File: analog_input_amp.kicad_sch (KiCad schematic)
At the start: 32 parts, among them U601 THS4521ID

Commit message: Schematic: add PNs for resistors
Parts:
- R601: Mfr (none) -> Bourns; Mfr PN (none) -> CR0805-J/-000ELF
- R602: Mfr (none) -> Bourns; Mfr PN (none) -> CR0805-FX-49R9ELF
- R603, R604: Mfr (none) -> Bourns; Mfr PN (none) -> CR0805-FX-1001ELF
- R605: Mfr (none) -> Bourns; Mfr PN (none) -> CR0805-FX-62R0ELF
- R606, R608: Mfr (none) -> Bourns; Mfr PN (none) -> CR0805-FX-2000ELF
- R607: Mfr (none) -> Bourns; Mfr PN (none) -> CR0805-FX-27R0ELF
- R609, R610: Mfr (none) -> Bourns; Mfr PN (none) -> CR0805-FX-24R0ELF
- R611, R612: Mfr (none) -> Bourns; Mfr PN (none) -> CR0805-FX-2200ELF
- R613, R614: Mfr (none) -> Bourns; Mfr PN (none) -> CR0805-FX-1000ELF
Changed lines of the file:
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@@
+      (effects (font (size 1.27 1.27)) hide)
+    )
+    (property "Mfr" "Bourns" (id 5) (at 156.21 106.68 0)
+      (effects (font (size 1.27 1.27)) hide)
+    )
+    (property "Mfr PN" "CR0805-FX-24R0ELF" (id 6) (at 156.21 106.68 0)
       (effects (font (size 1.27 1.27)) hide)
     )
@@
       (effects (font (size 1.27 1.27)) hide)
     )
+    (property "Mfr" "Bourns" (id 5) (at 167.64 125.73 0)
+      (effects (font (size 1.27 1.27)) hide)
+    )
+    (property "Mfr PN" "CR0805-FX-2200ELF" (id 6) (at 167.64 125.73 0)
+      (effects (font (size 1.27 1.27)) hide)
+    )
     (pin "1")
     (pin "2")
@@
     )
     (property "Tolerance" "" (id 4) (at 76.2 91.44 0)
+      (effects (font (size 1.27 1.27)) hide)
+    )
+    (property "Mfr" "Bourns" (id 5) (at 76.2 91.44 0)
+      (effects (font (size 1.27 1.27)) hide)
+    )
+    (property "Mfr PN" "CR0805-FX-49R9ELF" (id 6) (at 76.2 91.44 0)
       (effects (font (size 1.27 1.27)) hide)
     )
@@
       (effects (font (size 1.27 1.27)) hide)
     )
+    (property "Mfr" "Bourns" (id 5) (at 127 106.68 0)
+      (effects (font (size 1.27 1.27)) hide)
+    )
+    (property "Mfr PN" "CR0805-FX-27R0ELF" (id 6) (at 127 106.68 0)
+      (effects (font (size 1.27 1.27)) hide)
+    )
     (pin "1")
     (pin "2")
@@
     )
     (property "Tolerance" "" (id 4) (at 88.9 158.75 0)
+      (effects (font (size 1.27 1.27)) hide)
+    )
+    (property "Mfr" "Bourns" (id 5) (at 88.9 158.75 0)
+      (effects (font (size 1.27 1.27)) hide)
+    )
+    (property "Mfr PN" "CR0805-FX-1001ELF" (id 6) (at 88.9 158.75 0)
       (effects (font (size 1.27 1.27)) hide)
     )
@@
       (effects (font (size 1.27 1.27)) hide)
     )
+    (property "Mfr" "Bourns" (id 5) (at 167.64 45.72 0)
+      (effects (font (size 1.27 1.27)) hide)
+    )
+    (property "Mfr PN" "CR0805-FX-2200ELF" (id 6) (at 167.64 45.72 0)
+      (effects (font (size 1.27 1.27)) hide)
+    )
     (pin "1")
     (pin "2")
@@
       (effects (font (size 1.27 1.27)) hide)
     )
+    (property "Mfr" "Bourns" (id 5) (at 156.21 63.5 0)
+      (effects (font (size 1.27 1.27)) hide)
+    )
+    (property "Mfr PN" "CR0805-FX-24R0ELF" (id 6) (at 156.21 63.5 0)
+      (effects (font (size 1.27 1.27)) hide)
+    )
     (pin "1")
     (pin "2")
@@
     )
     (property "Tolerance" "" (id 4) (at 196.85 106.68 0)
+      (effects (font (size 1.27 1.27)) hide)
+    )
+    (property "Mfr" "Bourns" (id 5) (at 196.85 106.68 0)
+      (effects (font (size 1.27 1.27)) hide)
+    )
+    (property "Mfr PN" "CR0805-FX-1000ELF" (id 6) (at 196.85 106.68 0)
       (effects (font (size 1.27 1.27)) hide)
     )
@@
       (effects (font (size 1.27 1.27)) hide)
     )
+    (property "Mfr" "Bourns" (id 5) (at 139.7 106.68 0)
+      (effects (font (size 1.27 1.27)) hide)
+    )
+    (property "Mfr PN" "CR0805-FX-2000ELF" (id 6) (at 139.7 106.68 0)
+      (effects (font (size 1.27 1.27)) hide)
+    )
     (pin "1")
     (pin "2")
@@
       (effects (font (size 1.27 1.27)) hide)
     )
+    (property "Mfr" "Bourns" (id 5) (at 127 63.5 0)
+      (effects (font (size 1.27 1.27)) hide)
+    )
+    (property "Mfr PN" "CR0805-FX-2000ELF" (id 6) (at 127 63.5 0)
+      (effects (font (size 1.27 1.27)) hide)
+    )
     (pin "1")
     (pin "2")
@@
     )
     (property "Datasheet" "~" (id 3) (at 63.5 146.05 0)
+      (effects (font (size 1.27 1.27)) hide)
+    )
+    (property "Mfr" "Bourns" (id 4) (at 63.5 146.05 0)
+      (effects (font (size 1.27 1.27)) hide)
+    )
+    (property "Mfr PN" "CR0805-J/-000ELF" (id 5) (at 63.5 146.05 0)
       (effects (font (size 1.27 1.27)) hide)
     )
@@
       (effects (font (size 1.27 1.27)) hide)
     )
+    (property "Mfr" "Bourns" (id 5) (at 196.85 63.5 0)
+      (effects (font (size 1.27 1.27)) hide)
+    )
+    (property "Mfr PN" "CR0805-FX-1000ELF" (id 6) (at 196.85 63.5 0)
+      (effects (font (size 1.27 1.27)) hide)
+    )
     (pin "1")
     (pin "2")
@@
     )
     (property "Tolerance" "" (id 4) (at 88.9 146.05 0)
+      (effects (font (size 1.27 1.27)) hide)
+    )
+    (property "Mfr" "Bourns" (id 5) (at 88.9 146.05 0)
+      (effects (font (size 1.27 1.27)) hide)
+    )
+    (property "Mfr PN" "CR0805-FX-1001ELF" (id 6) (at 88.9 146.05 0)
       (effects (font (size 1.27 1.27)) hide)
     )
@@
       (effects (font (size 1.27 1.27)) hide)
     )
+    (property "Mfr" "Bourns" (id 5) (at 101.6 85.09 0)
+      (effects (font (size 1.27 1.27)) hide)
+    )
+    (property "Mfr PN" "CR0805-FX-62R0ELF" (id 6) (at 101.6 85.09 0)
+      (effects (font (size 1.27 1.27)) hide)
+    )

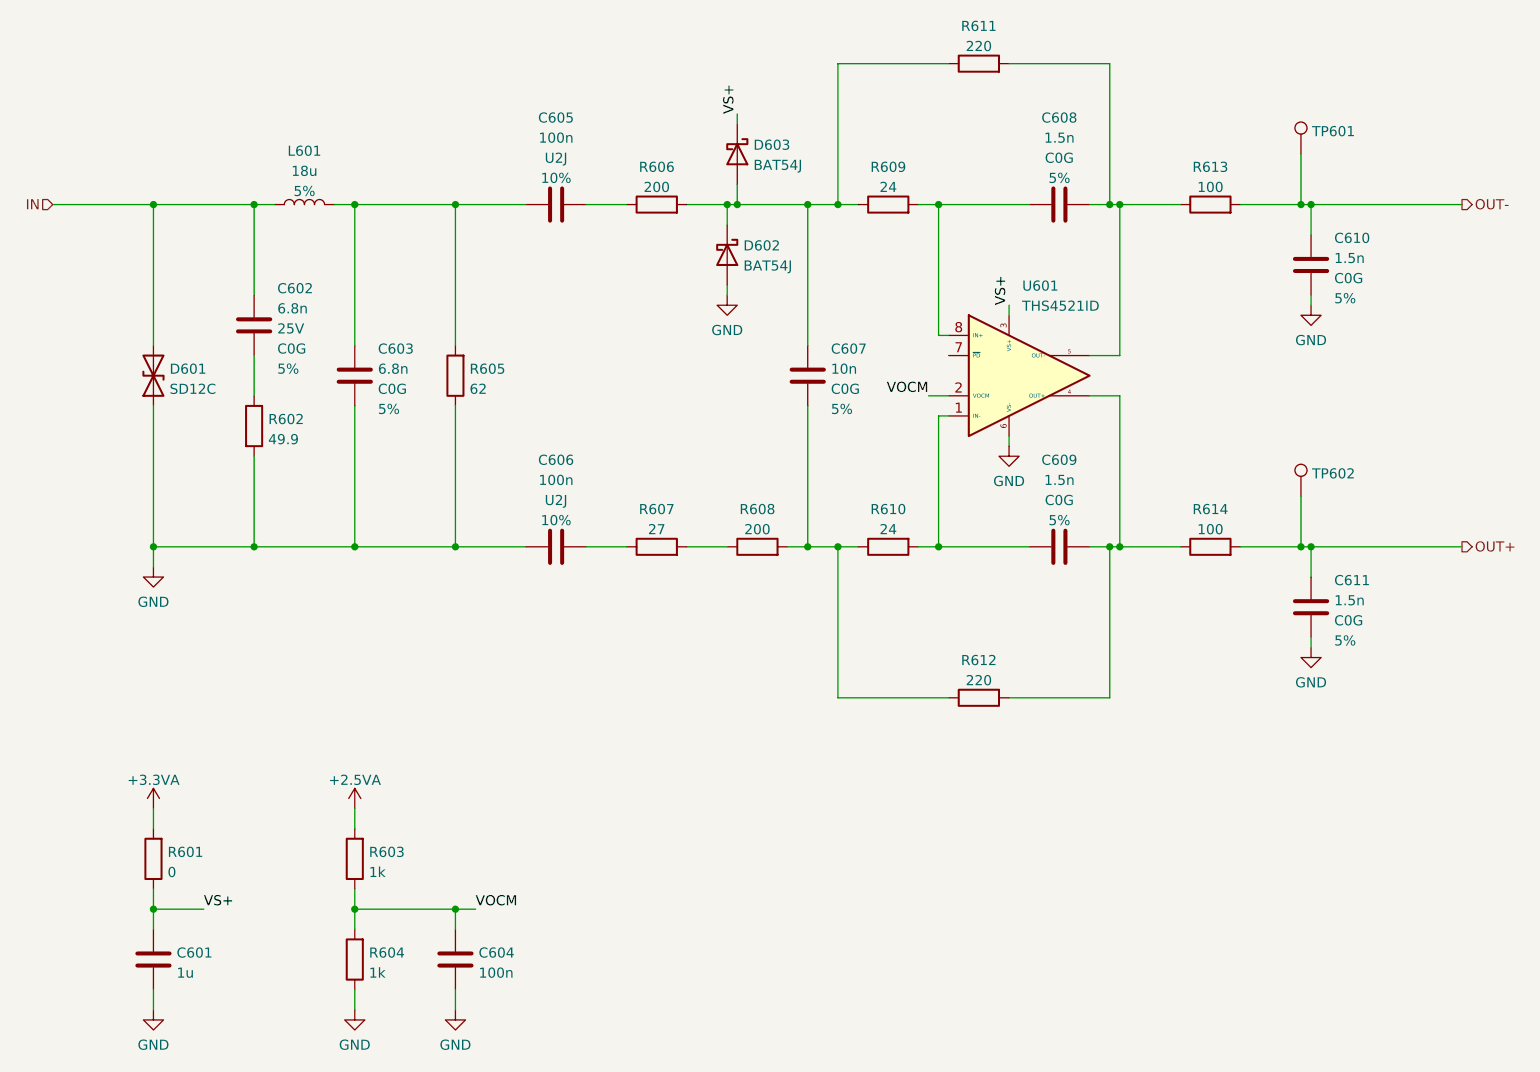
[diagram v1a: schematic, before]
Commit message: Combined update (kicad 6.0.4..) - Update schematic to kicad 6.0.4 - Assign footprints for SMA connectors - Replace MCP1825T with MCP1824T (chip shortages..)
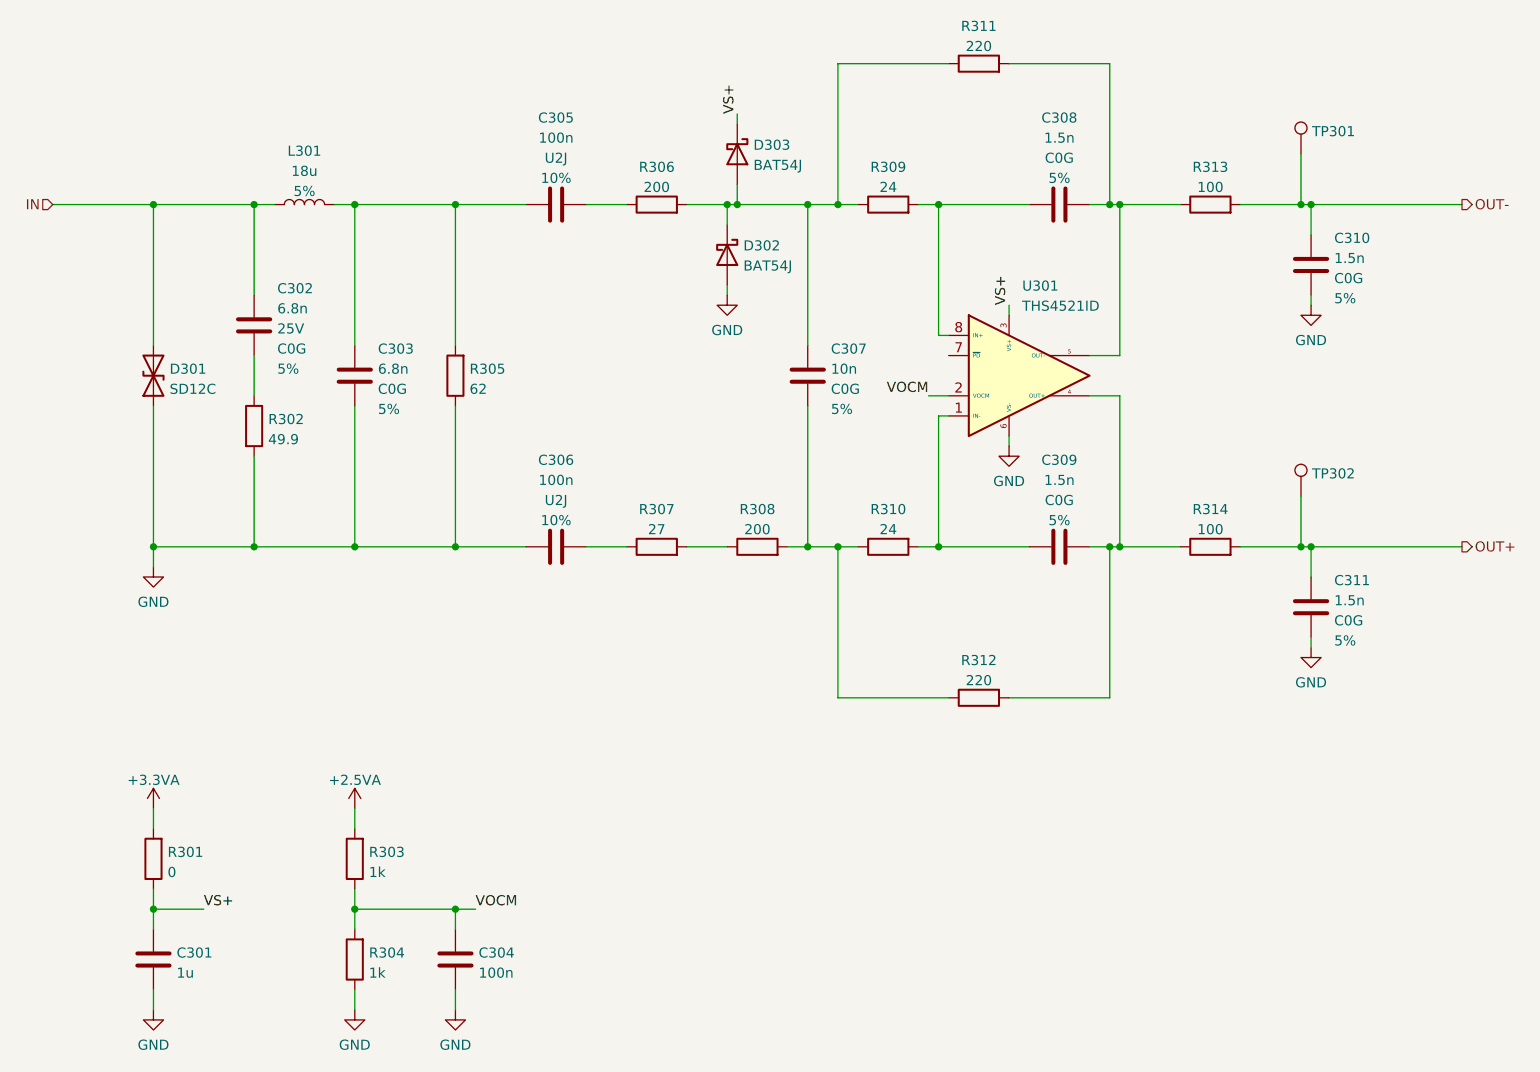
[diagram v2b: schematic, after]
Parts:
- renumbered C601 to C301, C602 to C302, C603 to C303, C604 to C304, C605 to C305, C606 to C306, C607 to C307, C608 to C308, C609 to C309, C610 to C310, C611 to C311, D601 to D301, D602 to D302, D603 to D303, L601 to L301, R601 to R301, R602 to R302, R603 to R303, R604 to R304, R605 to R305, R606 to R306, R607 to R307, R608 to R308, R609 to R309, R610 to R310, R611 to R311, R612 to R312, R613 to R313, R614 to R314, TP601 to TP301, TP602 to TP302, U601 to U301

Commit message: Update footprints: - SOD323F, SOD323, SOD123W... intead of generic handsolder version - 3225 xtal - use handsolder footprint - do not use handsolder version for ferrite beads - use SOT-23-6 instead of TSOP-6
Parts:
- D301: footprint Diode_SMD:D_SOD-323_HandSoldering -> Diode_SMD:D_SOD-323
- D302, D303: footprint Diode_SMD:D_SOD-323_HandSoldering -> Diode_SMD:D_SOD-323F
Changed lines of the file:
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@@
       (effects (font (size 1.27 1.27)) (justify left))
     )
-    (property "Footprint" "Diode_SMD:D_SOD-323_HandSoldering" (id 2) (at 131.445 69.85 0)
+    (property "Footprint" "Diode_SMD:D_SOD-323F" (id 2) (at 131.445 69.85 0)
       (effects (font (size 1.27 1.27)) hide)
     )
@@
       (effects (font (size 1.27 1.27)) (justify right))
     )
-    (property "Footprint" "Diode_SMD:D_SOD-323_HandSoldering" (id 2) (at 63.5 85.09 0)
+    (property "Footprint" "Diode_SMD:D_SOD-323" (id 2) (at 63.5 85.09 0)
       (effects (font (size 1.27 1.27)) hide)
     )
@@
       (effects (font (size 1.27 1.27)) (justify left))
     )
-    (property "Footprint" "Diode_SMD:D_SOD-323_HandSoldering" (id 2) (at 132.715 57.15 0)
-      (effects (font (size 1.27 1.27)) hide)
-    )
+    (property "Footprint" "Diode_SMD:D_SOD-323F" (id 2) (at 132.715 57.15 0)
+      (effects (font (size 1.27 1.27)) hide)
+    )

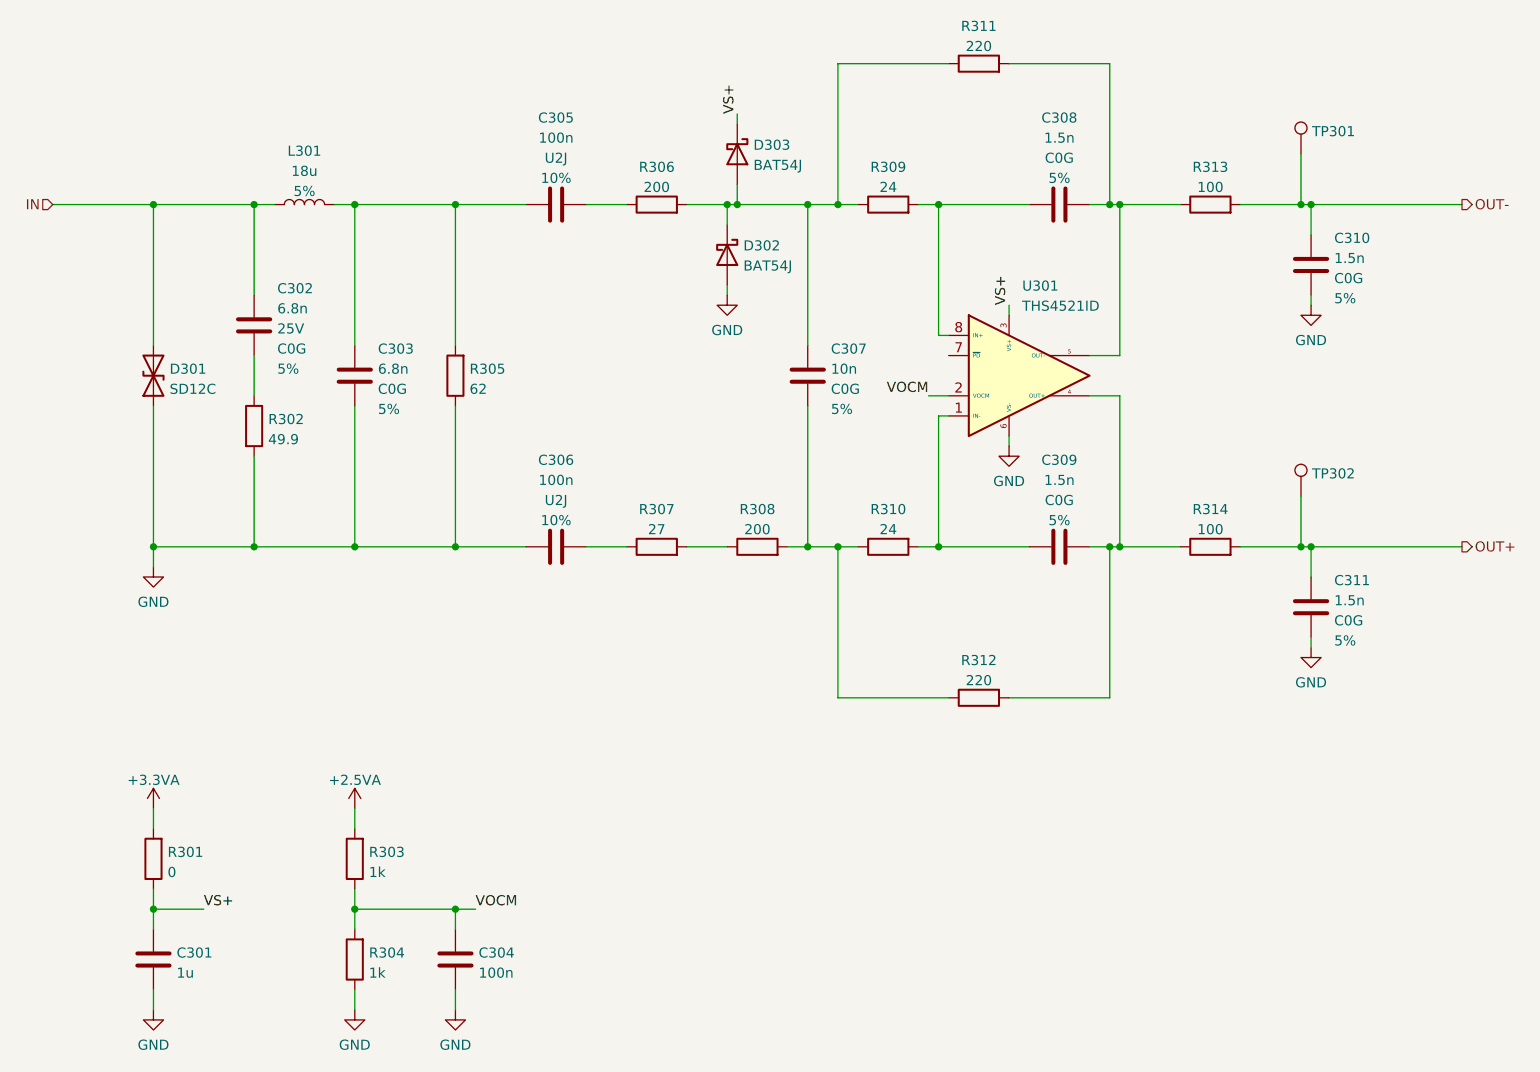
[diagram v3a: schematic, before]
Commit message: Redesign VOCM network, power FDA from 3v3 directly
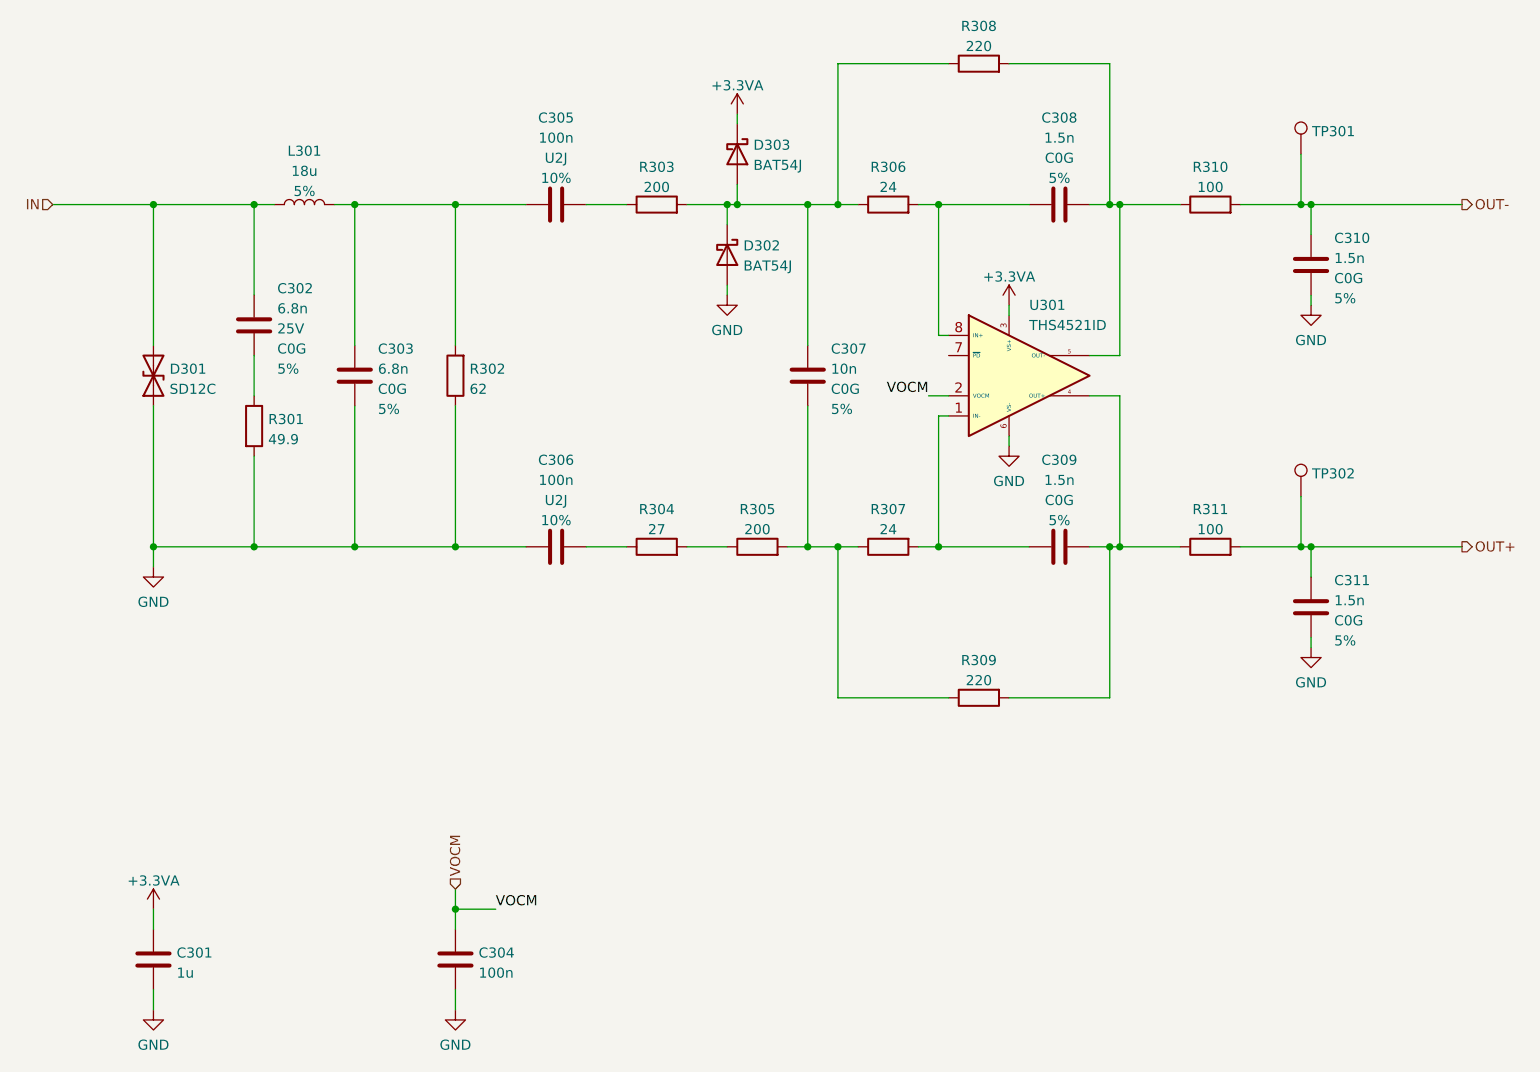
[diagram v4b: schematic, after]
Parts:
- removed R301: 0, Resistor_SMD:R_0805_2012Metric, symbol Device:R
- removed R303, R304: 1k, Resistor_SMD:R_0805_2012Metric, symbol Device:R
- renumbered R302 to R301, R305 to R302, R306 to R303, R307 to R304, R308 to R305, R309 to R306, R310 to R307, R311 to R308, R312 to R309, R313 to R310, R314 to R311
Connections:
- net VS+ is gone; now on net +3.3VA: C301.1, D303.1 (K), U301.3 (VS+)
